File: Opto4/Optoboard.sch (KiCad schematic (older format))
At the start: 39 parts, among them J1 S1 Connector, J2 S2 Connector, J3 S3 Connector, J4 S4 Connector, J5 Conn_01x06, Q1 IRLR024NPBF, U1 6N135, U2 6N135, U3 6N135, U4 6N135

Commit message: Changed some labels and text
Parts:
- D2, D3: footprint LEDs:LED_0805 -> LEDs:LED_1206
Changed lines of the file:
@@
 LIBS:contrib
 LIBS:valves
+LIBS:Optoboard-cache
 EELAYER 25 0
 EELAYER END
@@
 F 0 "D3" H 9300 1450 50  0000 C CNN
 F 1 "LED" H 9300 1250 50  0000 C CNN
-F 2 "LEDs:LED_0805" H 9300 1350 50  0001 C CNN
+F 2 "LEDs:LED_1206" H 9300 1350 50  0001 C CNN
 F 3 "" H 9300 1350 50  0001 C CNN
 	1    9300 1350
@@
 F 0 "D2" H 9100 1450 50  0000 C CNN
 F 1 "LED" H 9100 1250 50  0000 C CNN
-F 2 "LEDs:LED_0805" H 9100 1350 50  0001 C CNN
+F 2 "LEDs:LED_1206" H 9100 1350 50  0001 C CNN
 F 3 "" H 9100 1350 50  0001 C CNN
 	1    9100 1350

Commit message: Changed things that were discussed, also added photos
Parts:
- removed D3: LED, LEDs:LED_1206, symbol LED
- removed R22: R, Resistors_SMD:R_1206, symbol R
- D1: value D -> STTH2R06U
- D2: value LED -> LED_RED
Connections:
- wire segments 107 -> 103
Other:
- note added: "12V INPUT WITH DIODE PROTECTION"
- note added: "5V IN WITH MOSFET PROTECTION\n\n"
- note added: "LED FOR POWER"
- note added: "OPTO COUPLER CONNECTIONS TO FESTO SENSOR"
- note added: "SENSOR CONNECTOR\n"
- moved on the sheet: 12V_IN1, 5V_IN1, C1, C2, D1, D2, J1, J2, J3, J4, J5, R1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

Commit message: Added opto4 and opto6 updated images
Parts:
- J1, J2, J3, J4: footprint Connectors_Molex:Molex_KK-6410-03_03x2.54mm_Straight -> Connect:Wafer_Vertical10x5.8x7RM2.5-3
- R1, R10, R11, R12, R13, R14, R15, R16, R17, R18, R19, R2, R20, R21, R3, R4, R5, R6, R7, R8, R9: footprint Resistors_SMD:R_1206 -> Resistors_SMD:R_0805
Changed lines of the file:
@@
 LIBS:switches
 LIBS:relays
-LIBS:motors
 LIBS:transistors
 LIBS:conn
@@
 F 0 "J1" H 1150 1500 50  0000 C CNN
 F 1 "S1 Connector" V 1250 1300 50  0000 C CNN
-F 2 "Connectors_Molex:Molex_KK-6410-03_03x2.54mm_Straight" H 1150 1300 50  0001 C CNN
+F 2 "Connect:Wafer_Vertical10x5.8x7RM2.5-3" H 1150 1300 50  0001 C CNN
 F 3 "" H 1150 1300 50  0001 C CNN
 	1    1150 1300
@@
 F 0 "R1" V 1630 1200 50  0000 C CNN
 F 1 "0R" V 1550 1200 50  0000 C CNN
-F 2 "Resistors_SMD:R_1206" V 1480 1200 50  0001 C CNN
+F 2 "Resistors_SMD:R_0805" V 1480 1200 50  0001 C CNN
 F 3 "" H 1550 1200 50  0001 C CNN
 	1    1550 1200
@@
 F 0 "R2" V 1630 1400 50  0000 C CNN
 F 1 "0R" V 1550 1400 50  0000 C CNN
-F 2 "Resistors_SMD:R_1206" V 1480 1400 50  0001 C CNN
+F 2 "Resistors_SMD:R_0805" V 1480 1400 50  0001 C CNN
 F 3 "" H 1550 1400 50  0001 C CNN
 	1    1550 1400
@@
 F 0 "R5" V 1830 1000 50  0000 C CNN
 F 1 "100R" V 1750 1000 50  0000 C CNN
-F 2 "Resistors_SMD:R_1206" V 1680 1000 50  0001 C CNN
+F 2 "Resistors_SMD:R_0805" V 1680 1000 50  0001 C CNN
 F 3 "" H 1750 1000 50  0001 C CNN
 	1    1750 1000
@@
 F 0 "R6" V 1830 1600 50  0000 C CNN
 F 1 "100R" V 1750 1600 50  0000 C CNN
-F 2 "Resistors_SMD:R_1206" V 1680 1600 50  0001 C CNN
+F 2 "Resistors_SMD:R_0805" V 1680 1600 50  0001 C CNN
 F 3 "" H 1750 1600 50  0001 C CNN
 	1    1750 1600
@@
 F 0 "R9" V 2680 1250 50  0000 C CNN
 F 1 "4R7K" V 2600 1250 50  0000 C CNN
-F 2 "Resistors_SMD:R_1206" V 2530 1250 50  0001 C CNN
+F 2 "Resistors_SMD:R_0805" V 2530 1250 50  0001 C CNN
 F 3 "" H 2600 1250 50  0001 C CNN
 	1    2600 1250
@@
 F 0 "J3" H 3350 1450 50  0000 C CNN
 F 1 "S3 Connector" V 3450 1250 50  0000 C CNN
-F 2 "Connectors_Molex:Molex_KK-6410-03_03x2.54mm_Straight" H 3350 1250 50  0001 C CNN
+F 2 "Connect:Wafer_Vertical10x5.8x7RM2.5-3" H 3350 1250 50  0001 C CNN
 F 3 "" H 3350 1250 50  0001 C CNN
 	1    3350 1250
@@
 F 0 "R11" V 3830 1150 50  0000 C CNN
 F 1 "0R" V 3750 1150 50  0000 C CNN
-F 2 "Resistors_SMD:R_1206" V 3680 1150 50  0001 C CNN
+F 2 "Resistors_SMD:R_0805" V 3680 1150 50  0001 C CNN
 F 3 "" H 3750 1150 50  0001 C CNN
 	1    3750 1150
@@
 F 0 "R12" V 3830 1350 50  0000 C CNN
 F 1 "0R" V 3750 1350 50  0000 C CNN
-F 2 "Resistors_SMD:R_1206" V 3680 1350 50  0001 C CNN
+F 2 "Resistors_SMD:R_0805" V 3680 1350 50  0001 C CNN
 F 3 "" H 3750 1350 50  0001 C CNN
 	1    3750 1350
@@
 F 0 "R15" V 4030 950 50  0000 C CNN
 F 1 "100R" V 3950 950 50  0000 C CNN
-F 2 "Resistors_SMD:R_1206" V 3880 950 50  0001 C CNN
+F 2 "Resistors_SMD:R_0805" V 3880 950 50  0001 C CNN
 F 3 "" H 3950 950 50  0001 C CNN
 	1    3950 950
@@
 F 0 "R16" V 4030 1550 50  0000 C CNN
 F 1 "100R" V 3950 1550 50  0000 C CNN
-F 2 "Resistors_SMD:R_1206" V 3880 1550 50  0001 C CNN
+F 2 "Resistors_SMD:R_0805" V 3880 1550 50  0001 C CNN
 F 3 "" H 3950 1550 50  0001 C CNN
 	1    3950 1550
@@
 F 0 "R19" V 4880 1200 50  0000 C CNN
 F 1 "4R7K" V 4800 1200 50  0000 C CNN
-F 2 "Resistors_SMD:R_1206" V 4730 1200 50  0001 C CNN
+F 2 "Resistors_SMD:R_0805" V 4730 1200 50  0001 C CNN
 F 3 "" H 4800 1200 50  0001 C CNN
 	1    4800 1200
@@
 F 0 "J2" H 1150 3100 50  0000 C CNN
 F 1 "S2 Connector" V 1250 2900 50  0000 C CNN
-F 2 "Connectors_Molex:Molex_KK-6410-03_03x2.54mm_Straight" H 1150 2900 50  0001 C CNN
+F 2 "Connect:Wafer_Vertical10x5.8x7RM2.5-3" H 1150 2900 50  0001 C CNN
 F 3 "" H 1150 2900 50  0001 C CNN
 	1    1150 2900
@@
 F 0 "R3" V 1630 2800 50  0000 C CNN
 F 1 "0R" V 1550 2800 50  0000 C CNN
-F 2 "Resistors_SMD:R_1206" V 1480 2800 50  0001 C CNN
+F 2 "Resistors_SMD:R_0805" V 1480 2800 50  0001 C CNN
 F 3 "" H 1550 2800 50  0001 C CNN
 	1    1550 2800
@@
 F 0 "R4" V 1630 3000 50  0000 C CNN
 F 1 "0R" V 1550 3000 50  0000 C CNN
-F 2 "Resistors_SMD:R_1206" V 1480 3000 50  0001 C CNN
+F 2 "Resistors_SMD:R_0805" V 1480 3000 50  0001 C CNN
 F 3 "" H 1550 3000 50  0001 C CNN
 	1    1550 3000
@@
 F 0 "R7" V 1830 2600 50  0000 C CNN
 F 1 "100R" V 1750 2600 50  0000 C CNN
-F 2 "Resistors_SMD:R_1206" V 1680 2600 50  0001 C CNN
+F 2 "Resistors_SMD:R_0805" V 1680 2600 50  0001 C CNN
 F 3 "" H 1750 2600 50  0001 C CNN
 	1    1750 2600
@@
 F 0 "R8" V 1830 3200 50  0000 C CNN
 F 1 "100R" V 1750 3200 50  0000 C CNN
-F 2 "Resistors_SMD:R_1206" V 1680 3200 50  0001 C CNN
+F 2 "Resistors_SMD:R_0805" V 1680 3200 50  0001 C CNN
 F 3 "" H 1750 3200 50  0001 C CNN
 	1    1750 3200
@@
 F 0 "R10" V 2680 2850 50  0000 C CNN
 F 1 "4R7K" V 2600 2850 50  0000 C CNN
-F 2 "Resistors_SMD:R_1206" V 2530 2850 50  0001 C CNN
+F 2 "Resistors_SMD:R_0805" V 2530 2850 50  0001 C CNN
 F 3 "" H 2600 2850 50  0001 C CNN
 	1    2600 2850
@@
 F 0 "J4" H 3350 3050 50  0000 C CNN
 F 1 "S4 Connector" V 3450 2850 50  0000 C CNN
-F 2 "Connectors_Molex:Molex_KK-6410-03_03x2.54mm_Straight" H 3350 2850 50  0001 C CNN
+F 2 "Connect:Wafer_Vertical10x5.8x7RM2.5-3" H 3350 2850 50  0001 C CNN
 F 3 "" H 3350 2850 50  0001 C CNN
 	1    3350 2850
@@
 F 0 "R13" V 3830 2750 50  0000 C CNN
 F 1 "0R" V 3750 2750 50  0000 C CNN
-F 2 "Resistors_SMD:R_1206" V 3680 2750 50  0001 C CNN
+F 2 "Resistors_SMD:R_0805" V 3680 2750 50  0001 C CNN
 F 3 "" H 3750 2750 50  0001 C CNN
 	1    3750 2750
@@
 F 0 "R14" V 3830 2950 50  0000 C CNN
 F 1 "0R" V 3750 2950 50  0000 C CNN
-F 2 "Resistors_SMD:R_1206" V 3680 2950 50  0001 C CNN
+F 2 "Resistors_SMD:R_0805" V 3680 2950 50  0001 C CNN
 F 3 "" H 3750 2950 50  0001 C CNN
 	1    3750 2950
@@
 F 0 "R17" V 4030 2550 50  0000 C CNN
 F 1 "100R" V 3950 2550 50  0000 C CNN
-F 2 "Resistors_SMD:R_1206" V 3880 2550 50  0001 C CNN
+F 2 "Resistors_SMD:R_0805" V 3880 2550 50  0001 C CNN
 F 3 "" H 3950 2550 50  0001 C CNN
 	1    3950 2550
@@
 F 0 "R18" V 4030 3150 50  0000 C CNN
 F 1 "100R" V 3950 3150 50  0000 C CNN
-F 2 "Resistors_SMD:R_1206" V 3880 3150 50  0001 C CNN
+F 2 "Resistors_SMD:R_0805" V 3880 3150 50  0001 C CNN
 F 3 "" H 3950 3150 50  0001 C CNN
 	1    3950 3150
@@
 F 0 "R20" V 4880 2800 50  0000 C CNN
 F 1 "4R7K" V 4800 2800 50  0000 C CNN
-F 2 "Resistors_SMD:R_1206" V 4730 2800 50  0001 C CNN
+F 2 "Resistors_SMD:R_0805" V 4730 2800 50  0001 C CNN
 F 3 "" H 4800 2800 50  0001 C CNN
 	1    4800 2800
@@
 F 0 "R21" V 5980 1050 50  0000 C CNN
 F 1 "R" V 5900 1050 50  0000 C CNN
-F 2 "Resistors_SMD:R_1206" V 5830 1050 50  0001 C CNN
+F 2 "Resistors_SMD:R_0805" V 5830 1050 50  0001 C CNN
 F 3 "" H 5900 1050 50  0001 C CNN
 	1    5900 1050

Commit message: Added output files for both version
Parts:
- removed 5V_IN1: Screw_Terminal_01x02, Connectors_Terminal_Blocks:TerminalBlock_4UCON_19963_02x3.5mm_Straight, symbol Screw_Terminal_01x02
- removed Q1: IRLR024NPBF, TO_SOT_Packages_SMD:TO-252-2, symbol IRLB8721PBF
- added U5: L7805, TO_SOT_Packages_SMD:TO-252-2Lead, symbol L7805
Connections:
- wire segments 103 -> 100
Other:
- moved on the sheet: 12V_IN1, C1, D1

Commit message: Added files
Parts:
- added P1: CONN_01X02, Pin_Headers:Pin_Header_Straight_1x02, symbol CONN_01X02
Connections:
- net +5V: now also P1.2 (P2); no longer J5.1 (Pin_1)
- new net: J5.1 (Pin_1), P1.1 (P1)
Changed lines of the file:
@@
 L +5V #PWR17
 U 1 1 59C91360
-P 5800 2550
-F 0 "#PWR17" H 5800 2400 50  0001 C CNN
-F 1 "+5V" H 5800 2690 50  0000 C CNN
-F 2 "" H 5800 2550 50  0001 C CNN
-F 3 "" H 5800 2550 50  0001 C CNN
-	1    5800 2550
+P 5800 2350
+F 0 "#PWR17" H 5800 2200 50  0001 C CNN
+F 1 "+5V" H 5800 2490 50  0000 C CNN
+F 2 "" H 5800 2350 50  0001 C CNN
+F 3 "" H 5800 2350 50  0001 C CNN
+	1    5800 2350
 	1    0    0    -1
 $EndComp
@@
 Wire Wire Line
 	5800 3100 5850 3100
-Wire Wire Line
-	5800 2550 5800 2600
 Wire Wire Line
 	5800 2600 5850 2600
@@
 Wire Wire Line
 	7350 1100 7100 1100
+$Comp
+L CONN_01X02 P1
+U 1 1 5A038EC9
+P 5550 2450
+F 0 "P1" H 5550 2600 50  0000 C CNN
+F 1 "CONN_01X02" V 5650 2450 50  0001 C CNN
+F 2 "Pin_Headers:Pin_Header_Straight_1x02" H 5550 2450 50  0001 C CNN
+F 3 "" H 5550 2450 50  0000 C CNN
+	1    5550 2450
+	-1   0    0    1
+$EndComp
+Wire Wire Line
+	5800 2600 5800 2500
+Wire Wire Line
+	5800 2500 5750 2500
+Wire Wire Line
+	5750 2400 5800 2400
+Wire Wire Line
+	5800 2400 5800 2350
 $EndSCHEMATC

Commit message: Modified to 3.3V and 5V compatibility
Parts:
- 12V_IN1: footprint Connectors_Terminal_Blocks:TerminalBlock_4UCON_19963_02x3.5mm_Straight -> Connectors_Terminal_Blocks:TerminalBlock_Pheonix_MKDS1.5-2pol
- U1, U2, U3, U4: symbol 6N135 -> 6N135-RESCUE-Optoboard
- U5: value L7805 -> LM2937ET-3.3; footprint TO_SOT_Packages_SMD:TO-252-2Lead -> TO_SOT_Packages_SMD:SOT-223
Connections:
- net +5V renamed +3V3
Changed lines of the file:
@@
 EESchema Schematic File Version 2
+LIBS:Optoboard-rescue
 LIBS:power
 LIBS:device
 LIBS:switches
 LIBS:relays
+LIBS:motors
 LIBS:transistors
 LIBS:conn
@@
 $EndDescr
 $Comp
-L 6N135 U1
+L 6N135-RESCUE-Optoboard U1
 U 1 1 59C8B84D
 P 2150 1300
@@
 F 0 "12V_IN1" H 7750 1200 50  0000 C CNN
 F 1 "Screw_Terminal_01x02" V 8000 1000 50  0000 C CNN
-F 2 "Connectors_Terminal_Blocks:TerminalBlock_4UCON_19963_02x3.5mm_Straight" H 7900 1100 50  0001 C CNN
+F 2 "Connectors_Terminal_Blocks:TerminalBlock_Pheonix_MKDS1.5-2pol" H 7900 1100 50  0001 C CNN
 F 3 "" H 7900 1100 50  0001 C CNN
 	1    7900 1100
@@
 F 3 "" H 7100 1450 50  0001 C CNN
 	1    7100 1450
-	1    0    0    -1
-$EndComp
-$Comp
-L +5V #PWR24
-U 1 1 59C8D32B
-P 7800 2600
-F 0 "#PWR24" H 7800 2450 50  0001 C CNN
-F 1 "+5V" H 7800 2740 50  0000 C CNN
-F 2 "" H 7800 2600 50  0001 C CNN
-F 3 "" H 7800 2600 50  0001 C CNN
-	1    7800 2600
-	1    0    0    -1
-$EndComp
-$Comp
-L +12V #PWR22
-U 1 1 59C8D351
-P 7100 1050
-F 0 "#PWR22" H 7100 900 50  0001 C CNN
-F 1 "+12V" H 7100 1190 50  0000 C CNN
-F 2 "" H 7100 1050 50  0001 C CNN
-F 3 "" H 7100 1050 50  0001 C CNN
-	1    7100 1050
 	1    0    0    -1
 $EndComp
@@
 NoConn ~ 2450 1200
 $Comp
-L +5V #PWR5
-U 1 1 59C9090A
-P 2600 1050
-F 0 "#PWR5" H 2600 900 50  0001 C CNN
-F 1 "+5V" H 2600 1190 50  0000 C CNN
-F 2 "" H 2600 1050 50  0001 C CNN
-F 3 "" H 2600 1050 50  0001 C CNN
-	1    2600 1050
-	1    0    0    -1
-$EndComp
-$Comp
 L GND #PWR6
 U 1 1 59C90BB5
@@
 F 3 "" H 2600 1550 50  0001 C CNN
 	1    2600 1550
-	1    0    0    -1
-$EndComp
-$Comp
-L +5V #PWR17
-U 1 1 59C91360
-P 5800 2350
-F 0 "#PWR17" H 5800 2200 50  0001 C CNN
-F 1 "+5V" H 5800 2490 50  0000 C CNN
-F 2 "" H 5800 2350 50  0001 C CNN
-F 3 "" H 5800 2350 50  0001 C CNN
-	1    5800 2350
 	1    0    0    -1
 $EndComp
@@
 S1
 $Comp
-L 6N135 U3
+L 6N135-RESCUE-Optoboard U3
 U 1 1 59C95703
 P 4350 1250
@@
 NoConn ~ 4650 1150
 $Comp
-L +5V #PWR13
-U 1 1 59C95753
-P 4800 1000
-F 0 "#PWR13" H 4800 850 50  0001 C CNN
-F 1 "+5V" H 4800 1140 50  0000 C CNN
-F 2 "" H 4800 1000 50  0001 C CNN
-F 3 "" H 4800 1000 50  0001 C CNN
-	1    4800 1000
-	1    0    0    -1
-$EndComp
-$Comp
 L GND #PWR14
 U 1 1 59C95759
@@
 S3
 $Comp
-L 6N135 U2
+L 6N135-RESCUE-Optoboard U2
 U 1 1 59C95B88
 P 2150 2900
@@
 NoConn ~ 2450 2800
 $Comp
-L +5V #PWR7
-U 1 1 59C95BD8
-P 2600 2650
-F 0 "#PWR7" H 2600 2500 50  0001 C CNN
-F 1 "+5V" H 2600 2790 50  0000 C CNN
-F 2 "" H 2600 2650 50  0001 C CNN
-F 3 "" H 2600 2650 50  0001 C CNN
-	1    2600 2650
-	1    0    0    -1
-$EndComp
-$Comp
 L GND #PWR8
 U 1 1 59C95BDE
@@
 S2
 $Comp
-L 6N135 U4
+L 6N135-RESCUE-Optoboard U4
 U 1 1 59C95BE5
 P 4350 2850
@@
 NoConn ~ 4650 2750
 $Comp
-L +5V #PWR15
-U 1 1 59C95C35
-P 4800 2600
-F 0 "#PWR15" H 4800 2450 50  0001 C CNN
-F 1 "+5V" H 4800 2740 50  0000 C CNN
-F 2 "" H 4800 2600 50  0001 C CNN
-F 3 "" H 4800 2600 50  0001 C CNN
-	1    4800 2600
-	1    0    0    -1
-$EndComp
-$Comp
 L GND #PWR16
 U 1 1 59C95C3B
@@
 F 3 "" H 5900 1600 50  0001 C CNN
 	1    5900 1600
-	1    0    0    -1
-$EndComp
-$Comp
-L +5V #PWR19
-U 1 1 59C992CF
-P 5900 850
-F 0 "#PWR19" H 5900 700 50  0001 C CNN
-F 1 "+5V" H 5900 990 50  0000 C CNN
-F 2 "" H 5900 850 50  0001 C CNN
-F 3 "" H 5900 850 50  0001 C CNN
-	1    5900 850
 	1    0    0    -1
 $EndComp
@@
 P 7200 2650
 F 0 "U5" H 7050 2775 50  0000 C CNN
-F 1 "L7805" H 7200 2775 50  0000 L CNN
-F 2 "TO_SOT_Packages_SMD:TO-252-2Lead" H 7225 2500 50  0001 L CIN
+F 1 "LM2937ET-3.3" H 7200 2775 50  0000 L CNN
+F 2 "TO_SOT_Packages_SMD:SOT-223" H 7225 2500 50  0001 L CIN
 F 3 "" H 7200 2600 50  0001 C CNN
 	1    7200 2650
@@
 Wire Wire Line
 	5800 2400 5800 2350
+$Comp
+L +12V #PWR22
+U 1 1 59C8D351
+P 7100 1050
+F 0 "#PWR22" H 7100 900 50  0001 C CNN
+F 1 "+12V" H 7100 1190 50  0000 C CNN
+F 2 "" H 7100 1050 50  0001 C CNN
+F 3 "" H 7100 1050 50  0001 C CNN
+	1    7100 1050
+	1    0    0    -1
+$EndComp
+$Comp
+L +3.3V #PWR?
+U 1 1 5A5FB2A2
+P 7800 2600
+F 0 "#PWR?" H 7800 2450 50  0001 C CNN
+F 1 "+3.3V" H 7800 2740 50  0000 C CNN
+F 2 "" H 7800 2600 50  0001 C CNN
+F 3 "" H 7800 2600 50  0001 C CNN
+	1    7800 2600
+	1    0    0    -1
+$EndComp
+$Comp
+L +3.3V #PWR?
+U 1 1 5A5FB392
+P 5800 2350
+F 0 "#PWR?" H 5800 2200 50  0001 C CNN
+F 1 "+3.3V" H 5800 2490 50  0000 C CNN
+F 2 "" H 5800 2350 50  0001 C CNN
+F 3 "" H 5800 2350 50  0001 C CNN
+	1    5800 2350
+	1    0    0    -1
+$EndComp
+$Comp
+L +3.3V #PWR?
+U 1 1 5A5FB47B
+P 5900 850
+F 0 "#PWR?" H 5900 700 50  0001 C CNN
+F 1 "+3.3V" H 5900 990 50  0000 C CNN
+F 2 "" H 5900 850 50  0001 C CNN
+F 3 "" H 5900 850 50  0001 C CNN
+	1    5900 850
+	1    0    0    -1
+$EndComp
+$Comp
+L +3.3V #PWR?
+U 1 1 5A5FB78F
+P 4800 1000
+F 0 "#PWR?" H 4800 850 50  0001 C CNN
+F 1 "+3.3V" H 4800 1140 50  0000 C CNN
+F 2 "" H 4800 1000 50  0001 C CNN
+F 3 "" H 4800 1000 50  0001 C CNN
+	1    4800 1000
+	1    0    0    -1
+$EndComp
+$Comp
+L +3.3V #PWR?
+U 1 1 5A5FBA34
+P 4800 2600
+F 0 "#PWR?" H 4800 2450 50  0001 C CNN
+F 1 "+3.3V" H 4800 2740 50  0000 C CNN
+F 2 "" H 4800 2600 50  0001 C CNN
+F 3 "" H 4800 2600 50  0001 C CNN
+	1    4800 2600
+	1    0    0    -1
+$EndComp
+$Comp
+L +3.3V #PWR?
+U 1 1 5A5FBC45
+P 2600 2650
+F 0 "#PWR?" H 2600 2500 50  0001 C CNN
+F 1 "+3.3V" H 2600 2790 50  0000 C CNN
+F 2 "" H 2600 2650 50  0001 C CNN
+F 3 "" H 2600 2650 50  0001 C CNN
+	1    2600 2650
+	1    0    0    -1
+$EndComp
+$Comp
+L +3.3V #PWR?
+U 1 1 5A5FBD5E
+P 2600 1050
+F 0 "#PWR?" H 2600 900 50  0001 C CNN
+F 1 "+3.3V" H 2600 1190 50  0000 C CNN
+F 2 "" H 2600 1050 50  0001 C CNN
+F 3 "" H 2600 1050 50  0001 C CNN
+	1    2600 1050
+	1    0    0    -1
+$EndComp
 $EndSCHEMATC

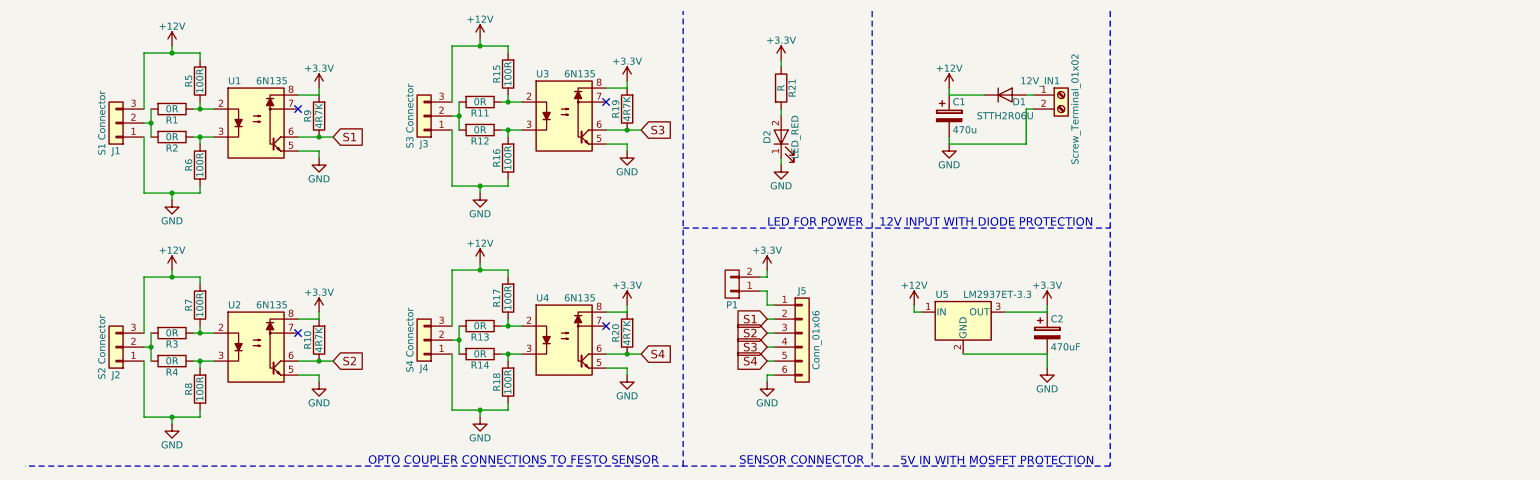
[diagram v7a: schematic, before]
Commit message: Updated the regulator and some small modifs
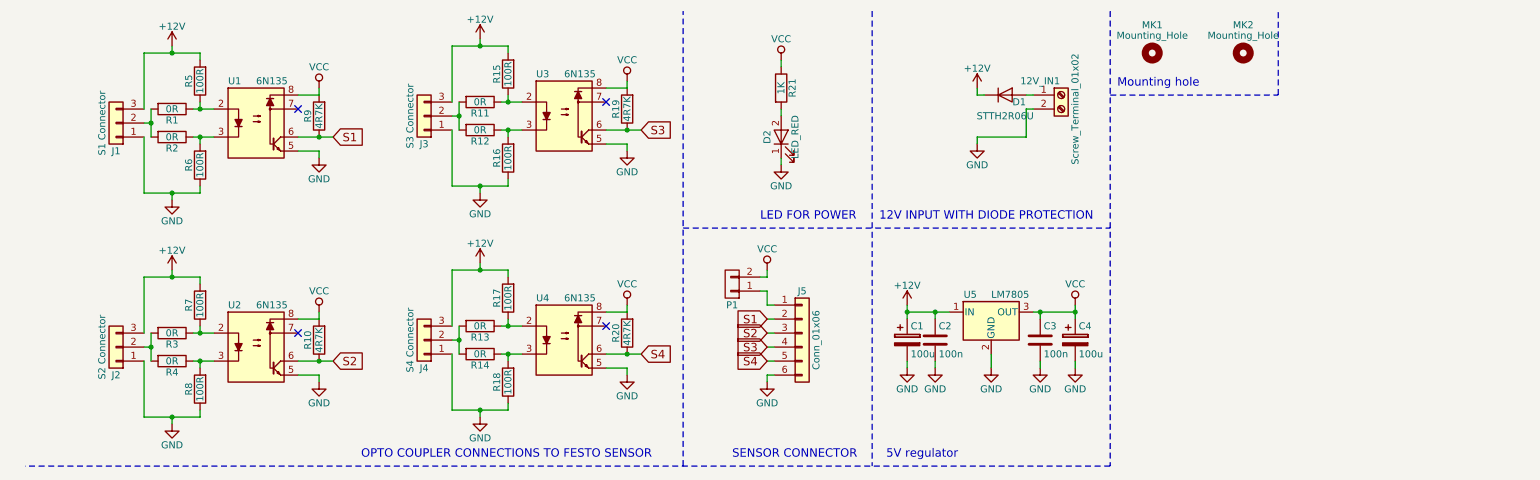
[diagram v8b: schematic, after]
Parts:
- removed C2: 470uF, Capacitors_SMD:CP_Elec_6.3x5.3, symbol CP
- added C2, C3: 100n, Capacitors_SMD:C_0805, symbol C
- added C4: 100u, Capacitors_SMD:CP_Elec_6.3x5.3, symbol CP
- added MK1, MK2: Mounting_Hole, Mounting_Holes:MountingHole_3.2mm_M3_Pad_Via, symbol Mounting_Hole
- C1: value 470u -> 100u
- R21: value R -> 1K
- U5: value LM2937ET-3.3 -> LM7805; footprint TO_SOT_Packages_SMD:SOT-223 -> TO_SOT_Packages_SMD:TO-252-2Lead
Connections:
- net +12V: now also C2.1
- net GND: now also C2.2, C3.2, C4.2
- net +3V3 renamed VCC
- net VCC: now also C3.1, C4.1
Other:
- note added: "5V regulator"
- note added: "Mounting hole"
- note removed: "5V IN WITH MOSFET PROTECTION\n\n"
- moved on the sheet: C1, U5
